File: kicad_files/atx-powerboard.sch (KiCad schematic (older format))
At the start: 2 parts

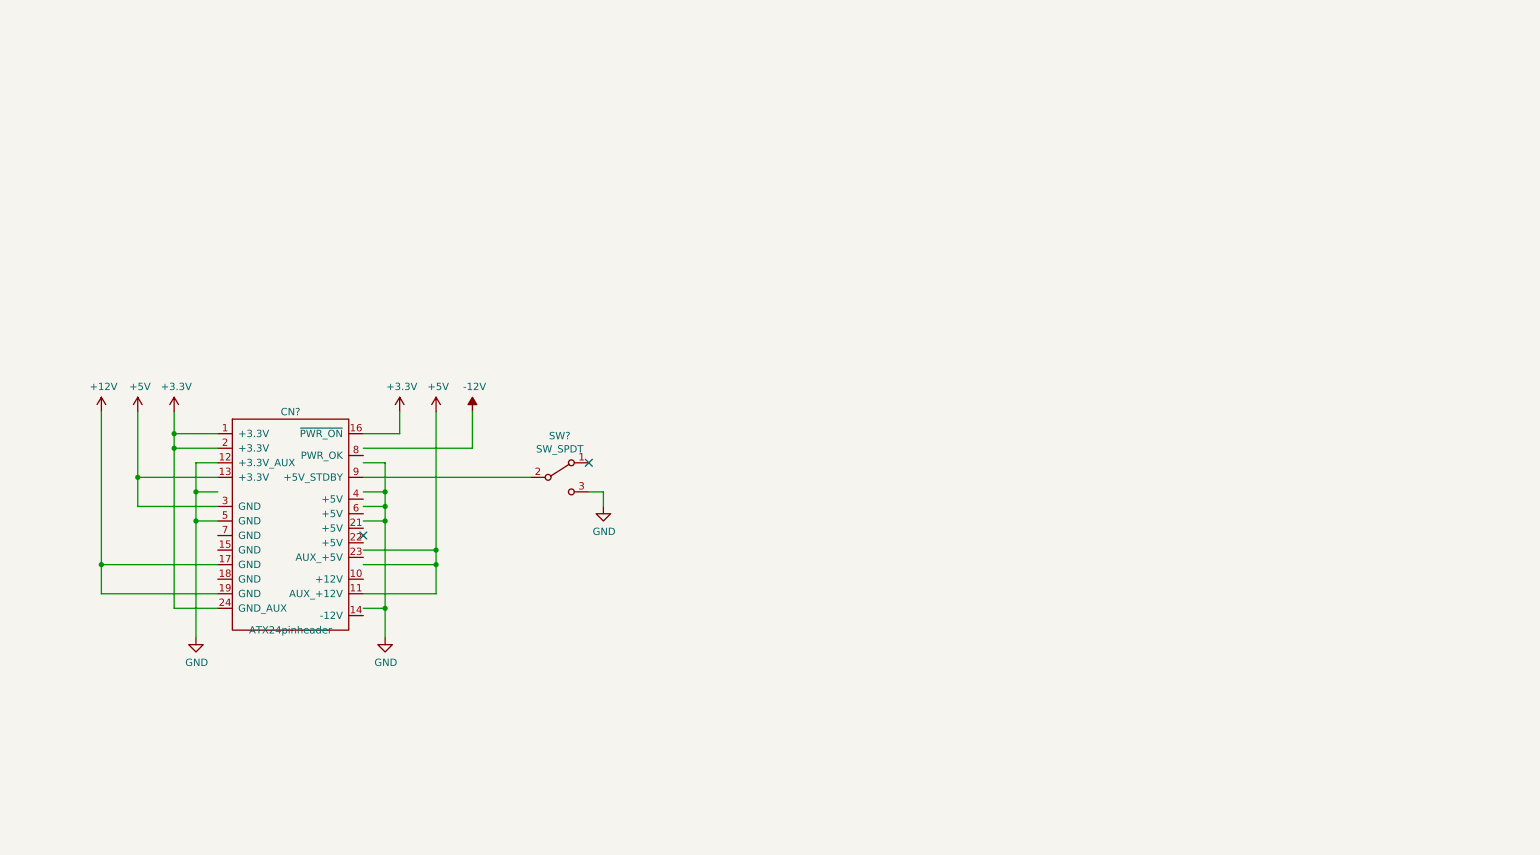
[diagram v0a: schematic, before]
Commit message: Changed layout of ATX for a v1
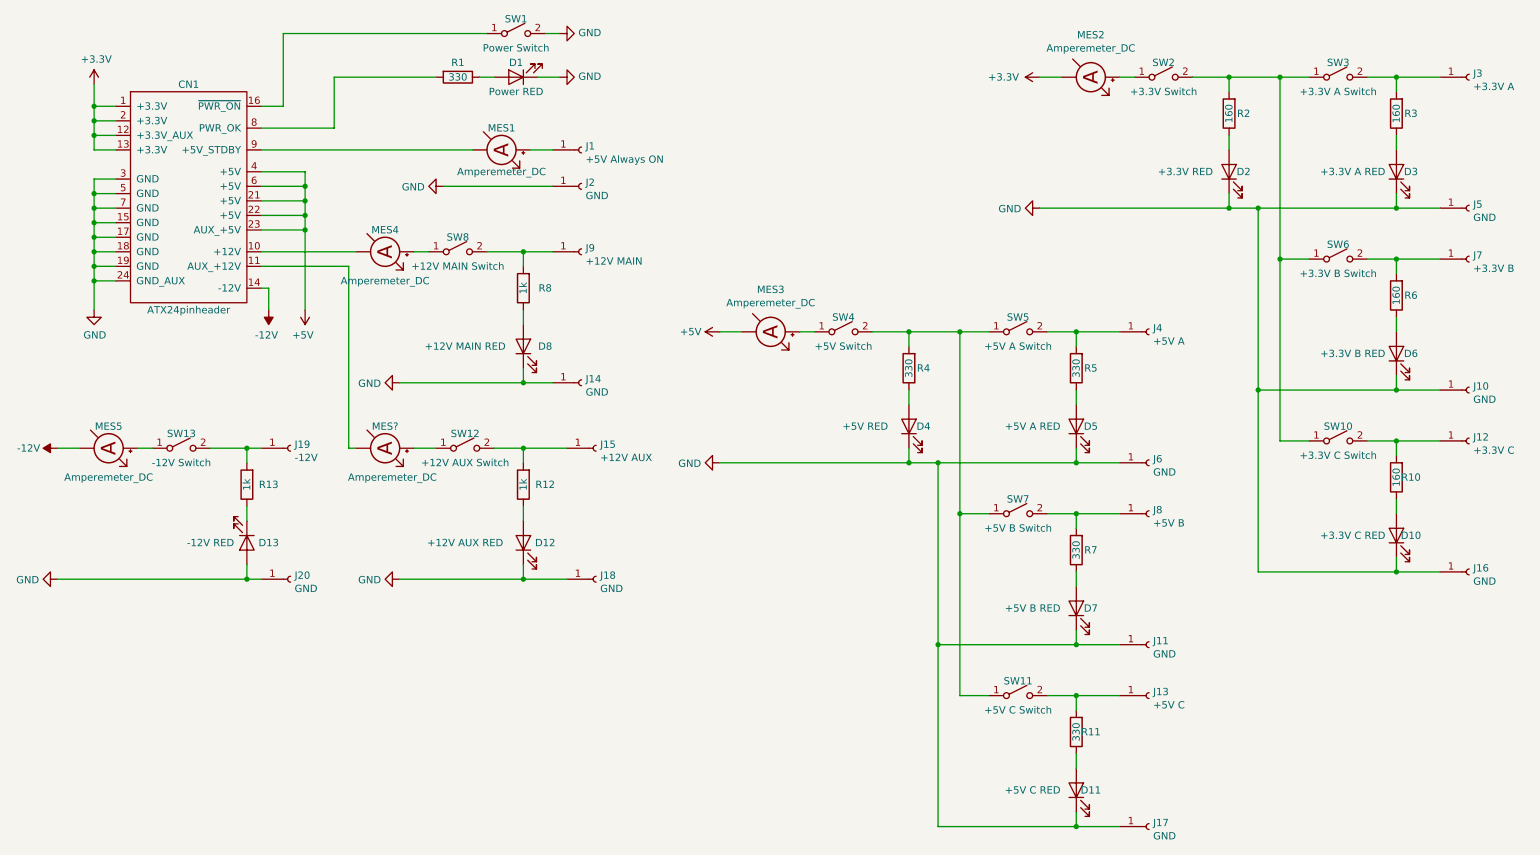
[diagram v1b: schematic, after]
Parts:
- removed SW?: SW_SPDT, symbol Switch:SW_SPDT
- added D1: Power RED, symbol Device:LED
- added D10: +3.3V C RED, symbol Device:LED
- added D11: +5V C RED, symbol Device:LED
- added D12: +12V AUX RED, symbol Device:LED
- added D13: -12V RED, symbol Device:LED
- added D2: +3.3V RED, symbol Device:LED
- added D3: +3.3V A RED, symbol Device:LED
- added D4: +5V RED, symbol Device:LED
- added D5: +5V A RED, symbol Device:LED
- added D6: +3.3V B RED, symbol Device:LED
- added D7: +5V B RED, symbol Device:LED
- added D8: +12V MAIN RED, symbol Device:LED
- added J1: +5V Always ON, symbol Connector:Conn_01x01_Female
- added J10, J11, J14, J16, J17, J18, J2, J20, J5, J6: GND, symbol Connector:Conn_01x01_Female
- added J12: +3.3V C, symbol Connector:Conn_01x01_Female
- added J13: +5V C, symbol Connector:Conn_01x01_Female
- added J15: +12V AUX, symbol Connector:Conn_01x01_Female
- added J19: -12V, symbol Connector:Conn_01x01_Female
- added J3: +3.3V A, symbol Connector:Conn_01x01_Female
- added J4: +5V A, symbol Connector:Conn_01x01_Female
- added J7: +3.3V B, symbol Connector:Conn_01x01_Female
- added J8: +5V B, symbol Connector:Conn_01x01_Female
- added J9: +12V MAIN, symbol Connector:Conn_01x01_Female
- added MES1, MES2, MES3, MES4, MES5, MES?: Amperemeter_DC, symbol Device:Amperemeter_DC
- added R1, R11, R4, R5, R7: 330, symbol Device:R
- added R10, R2, R3, R6: 160, symbol Device:R
- added R12, R13, R8: 1k, symbol Device:R
- added SW1: Power Switch, symbol Switch:SW_SPST
- added SW10: +3.3V C Switch, symbol Switch:SW_SPST
- added SW11: +5V C Switch, symbol Switch:SW_SPST
- added SW12: +12V AUX Switch, symbol Switch:SW_SPST
- added SW13: -12V Switch, symbol Switch:SW_SPST
- added SW2: +3.3V Switch, symbol Switch:SW_SPST
- added SW3: +3.3V A Switch, symbol Switch:SW_SPST
- added SW4: +5V Switch, symbol Switch:SW_SPST
- added SW5: +5V A Switch, symbol Switch:SW_SPST
- added SW6: +3.3V B Switch, symbol Switch:SW_SPST
- added SW7: +5V B Switch, symbol Switch:SW_SPST
- added SW8: +12V MAIN Switch, symbol Switch:SW_SPST
- gave numbers to parts that had none: 1
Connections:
- net labels removed: +12V
- wire segments 43 -> 151
- no-connect marks 2 -> 0
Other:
- moved on the sheet: CN1
